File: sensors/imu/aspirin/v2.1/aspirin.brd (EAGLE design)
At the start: 18.8 x 15.5 mm, 23 parts, among them IC1 LP2992, IC2 MS5611, IC3 >4KBIT SERIAL EEPROM HALF PRO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, U1 HMC5883, U2 MPU-6000

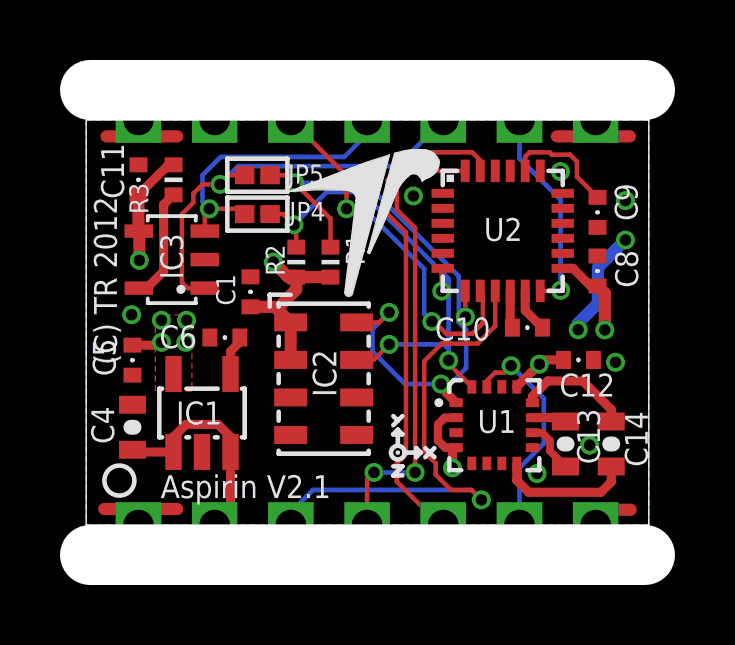
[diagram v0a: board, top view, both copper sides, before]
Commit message: Aspirin alt design is cleaner, made it the official routing of v2.1.
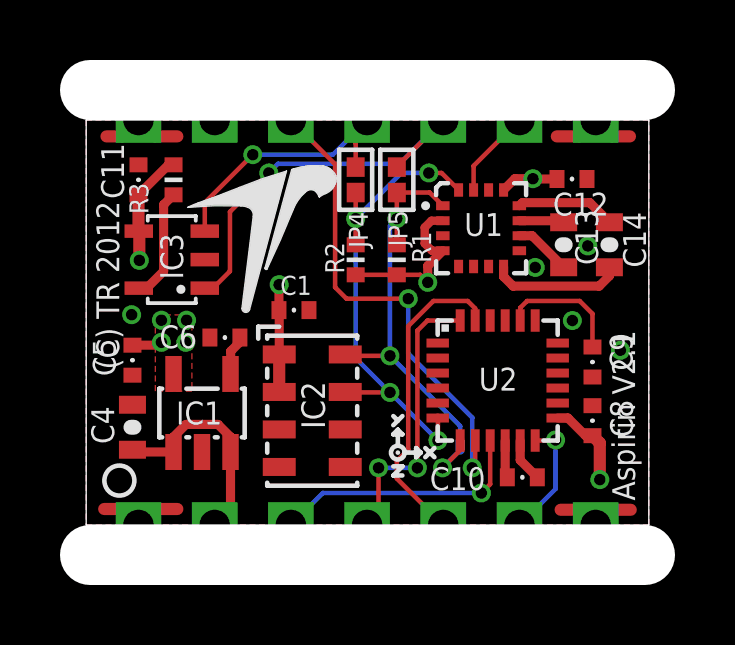
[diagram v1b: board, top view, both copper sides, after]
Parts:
- moved C13 6.64 mm to (14.2, 9.34)
- moved C14 6.64 mm to (15.7, 9.34)
- moved U1 6.58 mm to (11.4, 9.89)
- moved C12 6.04 mm to (14.4, 11.5)
- moved C10 4.99 mm to (12.8, 1.59)
- moved C8 4.99 mm to (15.1, 3.48)
- moved C9 4.99 mm to (15.1, 5.43)
- moved U2 4.99 mm to (12.0, 4.82)
- moved JP5 4.65 mm to (8.61, 11.5), turned to 270 degrees
- moved U$1 3.47 mm to (4.11, 9.53)
- moved JP4 3.47 mm to (7.24, 11.5), turned to 270 degrees
- moved R1 2.21 mm to (8.61, 8.84)
- moved R2 1.98 mm to (7.24, 8.84)
- moved C1 1.57 mm to (5.18, 7.16), turned to 0 degrees
- moved IC2 1.13 mm to (5.79, 3.81)
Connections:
- net GYRO_INT: now also U1.15; no longer U2.12
- net MAG_INT: now also U2.12; no longer U1.15
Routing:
- net MISO: track 17.1 -> 8.66 mm
- net SCL: track 22.0 -> 15.7 mm, vias 4 -> 3
- net MOSI: track 15.5 -> 9.50 mm
- net SCK: track 16.5 -> 10.5 mm
- net ACC_CS: track 12.1 -> 16.3 mm
- net GYRO_INT: track 6.93 -> 2.97 mm, vias 1 -> 0
- net MAG_INT: track 7.32 -> 4.02 mm
- net GND: track 16.2 -> 14.4 mm, vias 9 -> 5
- net SDA: track 18.4 -> 16.8 mm
- net XSCL: track 14.3 -> 13.6 mm
- net XSDA: track 9.79 -> 9.24 mm
- net N$48: track 3.84 -> 3.31 mm
